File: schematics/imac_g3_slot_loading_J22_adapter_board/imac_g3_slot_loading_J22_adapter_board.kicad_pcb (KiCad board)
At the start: 2 copper layers, 61.3 x 30 mm, 8 parts, among them J1 Conn_02x13_Odd_Even, J2 AC Power, J3 Conn_01x04_Male, J4 Conn_01x04_Male, J5 Conn_01x04_Male

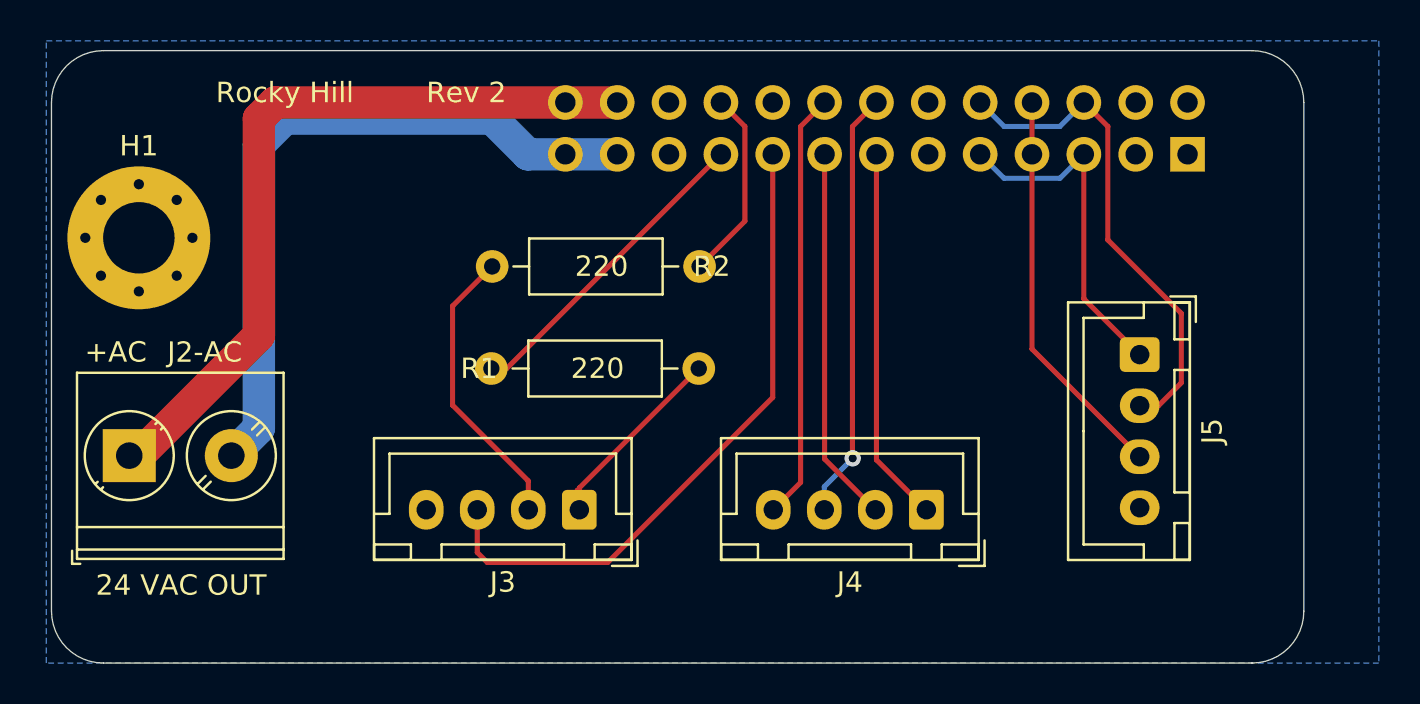
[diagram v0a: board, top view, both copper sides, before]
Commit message: Headphone sense
Added second sense wire from j22 board since they can't be combined.
Send sense inputs to arduino and control SE/~BTL signal from there. This will allow different volume settings for each mode.
Re-route.
Fix silkscreen labels
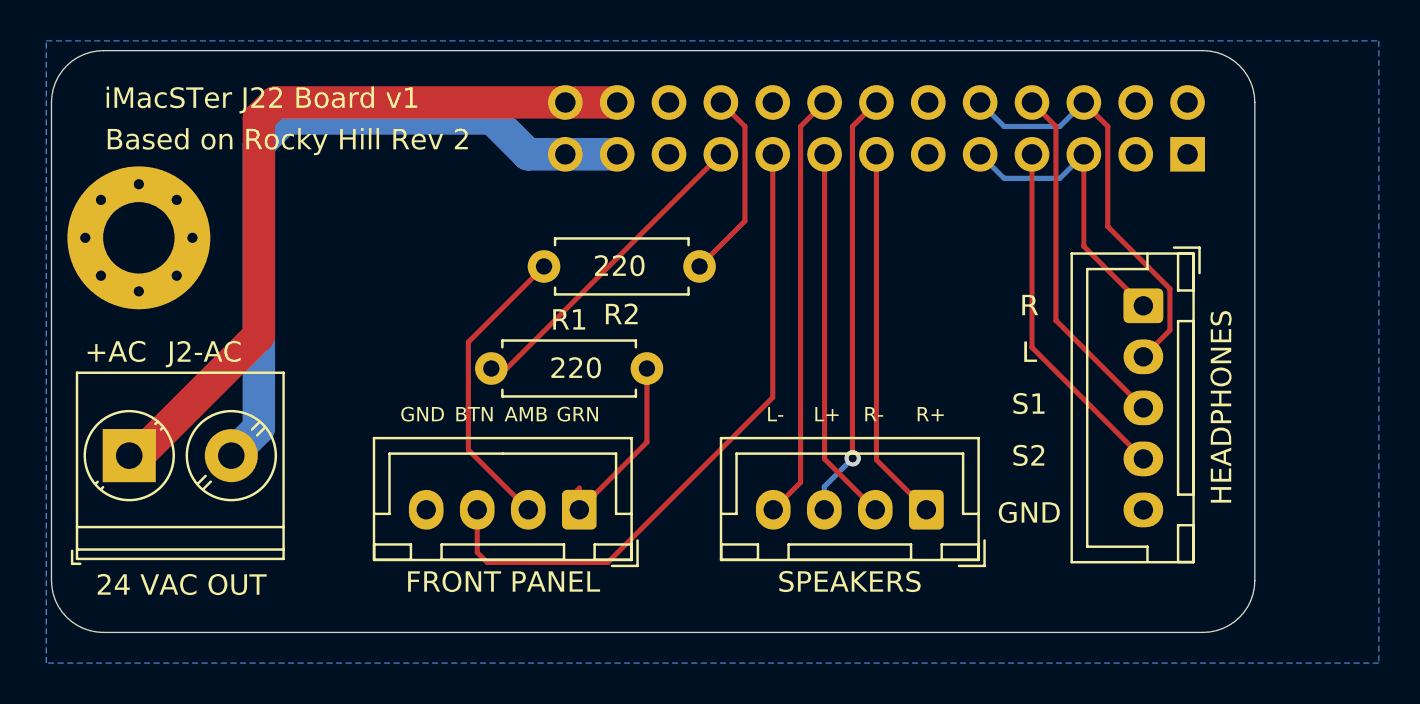
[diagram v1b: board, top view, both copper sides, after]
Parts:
- FRONT PANEL: renamed from J3
- HEADPHONES: renamed from J5; footprint Connector_JST:JST_XH_B4B-XH-A_1x04_P2.50mm_Vertical -> Connector_JST:JST_XH_B5B-XH-A_1x05_P2.50mm_Vertical
- R1, R2: footprint Resistor_THT:R_Axial_DIN0207_L6.3mm_D2.5mm_P10.16mm_Horizontal -> Resistor_THT:R_Axial_DIN0207_L6.3mm_D2.5mm_P7.62mm_Horizontal
- moved HEADPHONES 2.40 mm to (159.4, 99.4)
- renumbered J4 to SPEAKERS
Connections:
- HEADPHONES pad 4: GNDREF -> /HEADPHONE_2_SENSE
- J1 pad 7: /HEADPHONE_1_SENSE -> /HEADPHONE_2_SENSE
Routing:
- net /HEADPHONE_2_SENSE: track 0.00 -> 17.2 mm
- net /HEADPHONE_1_LEFT: track 24.3 -> 20.8 mm
- net /HEADPHONE_1_RIGHT: track 17.0 -> 14.7 mm
- net /HEADPHONE_1_SENSE: track 19.5 -> 18.1 mm
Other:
- board size 61.3 x 30 mm -> 58.9 x 28.5 mm
- board text added: "AMB"
- board text added: "BTN"
- board text added: "Based on Rocky Hill Rev 2"
- board text added: "GND"
- board text added: "GRN"
- board text added: "L"
- board text added: "L+"
- board text added: "L-"
- board text added: "R"
- board text added: "R+"
- board text added: "R-"
- board text added: "S1"
- board text added: "S2"
- board text added: "iMacSTer J22 Board v1"
- board text removed: "Rev 2"
- board text removed: "Rocky Hill"

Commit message: Code and schematic changes
Fixed incorrect routing for decoupling caps
Updated code to handle headphones, power button and mister buttons.
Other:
- rule pad_to_mask_clearance: 0.051 -> 0
- board text added: "JLCJLCJLCJLC"
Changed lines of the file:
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@@
   (general
     (thickness 1.6)
-    (drawings 28)
+    (drawings 29)
     (tracks 62)
     (zones 0)
@@
     (pad_size 1.7 1.7)
     (pad_drill 1)
-    (pad_to_mask_clearance 0.051)
-    (solder_mask_min_width 0.25)
+    (pad_to_mask_clearance 0)
     (aux_axis_origin 0 0)
     (grid_origin 106.04 116.64)
     (visible_elements FFFFFF7F)
     (pcbplotparams
-      (layerselection 0x010fc_ffffffff)
+      (layerselection 0x010e0_ffffffff)
       (usegerberextensions false)
       (usegerberattributes false)
@@
     (add_net /POWER_BUTTON)
     (add_net GNDREF)
-    (add_net "Net-(J1-Pad1)")
-    (add_net "Net-(J1-Pad12)")
-    (add_net "Net-(J1-Pad2)")
-    (add_net "Net-(J1-Pad21)")
-    (add_net "Net-(J1-Pad22)")
-    (add_net "Net-(J1-Pad3)")
     (add_net "Net-(J3-Pad1)")
     (add_net "Net-(J3-Pad2)")
@@
     )
     (fp_text value 220 (at 3.81 2.37) (layer F.Fab)
-      (effects (font (size 1 1) (thickness 0.15)))
-    )
-    (fp_text user %R (at 3.81 0) (layer F.Fab)
       (effects (font (size 1 1) (thickness 0.15)))
     )
@@
     (fp_line (start 8.67 1.5) (end 8.67 -1.5) (layer F.CrtYd) (width 0.05))
     (fp_line (start 8.67 -1.5) (end -1.05 -1.5) (layer F.CrtYd) (width 0.05))
+    (fp_text user %R (at 3.81 0) (layer F.Fab)
+      (effects (font (size 1 1) (thickness 0.15)))
+    )
     (pad 2 thru_hole oval (at 7.62 0 180) (size 1.6 1.6) (drill 0.8) (layers *.Cu *.Mask)
       (net 14 "Net-(J3-Pad2)"))
@@
     )
     (fp_text value 220 (at 3.81 2.37) (layer F.Fab)
-      (effects (font (size 1 1) (thickness 0.15)))
-    )
-    (fp_text user %R (at 3.81 0) (layer F.Fab)
       (effects (font (size 1 1) (thickness 0.15)))
     )
@@
     (fp_line (start 8.67 1.5) (end 8.67 -1.5) (layer F.CrtYd) (width 0.05))
     (fp_line (start 8.67 -1.5) (end -1.05 -1.5) (layer F.CrtYd) (width 0.05))
+    (fp_text user %R (at 3.81 0) (layer F.Fab)
+      (effects (font (size 1 1) (thickness 0.15)))
+    )
     (pad 2 thru_hole oval (at 7.62 0) (size 1.6 1.6) (drill 0.8) (layers *.Cu *.Mask)
       (net 15 "Net-(J3-Pad1)"))
@@
     )
     (fp_text value Conn_01x04_Male (at 5 4.6 90) (layer F.Fab)
-      (effects (font (size 1 1) (thickness 0.15)))
-    )
-    (fp_text user %R (at 5 2.7 90) (layer F.Fab)
       (effects (font (size 1 1) (thickness 0.15)))
     )
@@
     (fp_line (start -1.6 -2.75) (end -2.85 -2.75) (layer F.SilkS) (width 0.12))
     (fp_line (start -2.85 -2.75) (end -2.85 -1.5) (layer F.SilkS) (width 0.12))
+    (fp_text user %R (at 5 2.7 90) (layer F.Fab)
+      (effects (font (size 1 1) (thickness 0.15)))
+    )
     (pad 5 thru_hole oval (at 10 0 270) (size 1.7 1.95) (drill 0.95) (layers *.Cu *.Mask)
       (net 1 GNDREF))
@@
     (pad 2 thru_hole oval (at 2.5 0 270) (size 1.7 1.95) (drill 0.95) (layers *.Cu *.Mask)
       (net 4 /HEADPHONE_1_LEFT))
-    (pad 1 thru_hole roundrect (at 0 0 270) (size 1.7 1.95) (drill 0.95) (layers *.Cu *.Mask) (roundrect_rratio 0.147059)
+    (pad 1 thru_hole roundrect (at 0 0 270) (size 1.7 1.95) (drill 0.95) (layers *.Cu *.Mask) (roundrect_rratio 0.1470588235294118)
       (net 3 /HEADPHONE_1_RIGHT))
     (model ${KISYS3DMOD}/Connector_JST.3dshapes/JST_XH_B5B-XH-A_1x05_P2.50mm_Vertical.wrl
@@
     (pad 2 thru_hole oval (at 2.5 0 180) (size 1.7 1.95) (drill 0.95) (layers *.Cu *.Mask)
       (net 7 /-RIGHT_SPEAKER))
-    (pad 1 thru_hole roundrect (at 0 0 180) (size 1.7 1.95) (drill 0.95) (layers *.Cu *.Mask) (roundrect_rratio 0.147059)
+    (pad 1 thru_hole roundrect (at 0 0 180) (size 1.7 1.95) (drill 0.95) (layers *.Cu *.Mask) (roundrect_rratio 0.1470588235294118)
       (net 5 /+RIGHT_SPEAKER))
     (model ${KISYS3DMOD}/Connector_JST.3dshapes/JST_XH_B4B-XH-A_1x04_P2.50mm_Vertical.wrl
@@
     (pad 2 thru_hole oval (at 2.5 0 180) (size 1.7 1.95) (drill 0.95) (layers *.Cu *.Mask)
       (net 14 "Net-(J3-Pad2)"))
-    (pad 1 thru_hole roundrect (at 0 0 180) (size 1.7 1.95) (drill 0.95) (layers *.Cu *.Mask) (roundrect_rratio 0.147059)
+    (pad 1 thru_hole roundrect (at 0 0 180) (size 1.7 1.95) (drill 0.95) (layers *.Cu *.Mask) (roundrect_rratio 0.1470588235294118)
       (net 15 "Net-(J3-Pad1)"))
     (model ${KISYS3DMOD}/Connector_JST.3dshapes/JST_XH_B4B-XH-A_1x04_P2.50mm_Vertical.wrl
@@
       (net 1 GNDREF))
   )
+  (gr_text JLCJLCJLCJLC (at 118.74 101.908 90) (layer F.SilkS)
+    (effects (font (size 1 1) (thickness 0.15)))
+  )
   (gr_text GND (at 153.792 109.528) (layer F.SilkS)
     (effects (font (size 1 1) (thickness 0.15)))
@@
   (gr_line (start 105.892 89.408) (end 105.892 112.828) (layer Edge.Cuts) (width 0.05))
   (gr_line (start 162.3 86.868) (end 108.432 86.868) (layer Edge.Cuts) (width 0.05))
-  (segment (start 155.288999 93.123001) (end 156.464 91.948) (width 0.25) (layer B.Cu) (net 3))
-  (segment (start 152.559001 93.123001) (end 155.288999 93.123001) (width 0.25) (layer B.Cu) (net 3))
-  (segment (start 151.384 91.948) (end 152.559001 93.123001) (width 0.25) (layer B.Cu) (net 3))
   (segment (start 160.12 104.26) (end 159.2 104.26) (width 0.25) (layer F.Cu) (net 2))
   (segment (start 155.099001 90.583001) (end 155.099001 100.087001) (width 0.25) (layer F.Cu) (net 2))
   (segment (start 155.099001 100.087001) (end 159.38 104.368) (width 0.25) (layer F.Cu) (net 2))
   (segment (start 153.924 89.408) (end 155.099001 90.583001) (width 0.25) (layer F.Cu) (net 2))
+  (segment (start 155.288999 93.123001) (end 156.464 91.948) (width 0.25) (layer B.Cu) (net 3))
+  (segment (start 152.559001 93.123001) (end 155.288999 93.123001) (width 0.25) (layer B.Cu) (net 3))
+  (segment (start 151.384 91.948) (end 152.559001 93.123001) (width 0.25) (layer B.Cu) (net 3))
   (segment (start 156.464 96.452) (end 159.38 99.368) (width 0.25) (layer F.Cu) (net 3))
   (segment (start 156.464 91.948) (end 156.464 96.452) (width 0.25) (layer F.Cu) (net 3))

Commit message: Gerber Files
Exported gerber files for all PCBs
Updated main board to version 1.2 with fixes the routing that were bodged into previous version.
Updated to kicad 6
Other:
- net class Default removed
